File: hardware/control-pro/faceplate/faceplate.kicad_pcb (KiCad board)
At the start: 2 copper layers, 180 x 90 mm, 19 parts

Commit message: Enlarged 3rd slider slot width to remove copper from faceplate.
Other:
- board text added: "DMX-CPF, Rev 1.1 Crazy Giraffe Software"
- board text removed: "DMX-CPF, Rev 1.0 Crazy Giraffe Software"
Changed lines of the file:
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@@
     (title "DMX Demonstrator - Control-Pro Faceplate (DMX-CPF)")
     (date 2020-09-15)
-    (rev 1.0)
+    (rev 1.1)
     (company "Crazy Giraffe Software")
     (comment 2 "Designed by: SparkyBobo")
@@
     (fp_circle (center 0 0) (end 3.2 0) (layer Cmts.User) (width 0.15))
     (fp_circle (center 0 0) (end 3.45 0) (layer F.CrtYd) (width 0.05))
-    (pad "" np_thru_hole oval (at 0 6.25) (size 2.6 60) (drill oval 2 60) (layers *.Cu *.Mask))
+    (pad "" np_thru_hole oval (at 0 6.25) (size 2.6 60) (drill oval 2.6 60) (layers *.Cu *.Mask))
   )
   (module MountingHole:MountingHole_3.2mm_M3 (layer F.Cu)
@@
     (effects (font (size 1.5 1.5) (thickness 0.3)))
   )
-  (gr_text "DMX-CPF, Rev 1.0\nCrazy Giraffe Software" (at 240.75 72.25 90) (layer B.SilkS)
+  (gr_text "DMX-CPF, Rev 1.1\nCrazy Giraffe Software" (at 240.75 72.25 90) (layer B.SilkS)
     (effects (font (size 1 1) (thickness 0.15)) (justify mirror))
   )

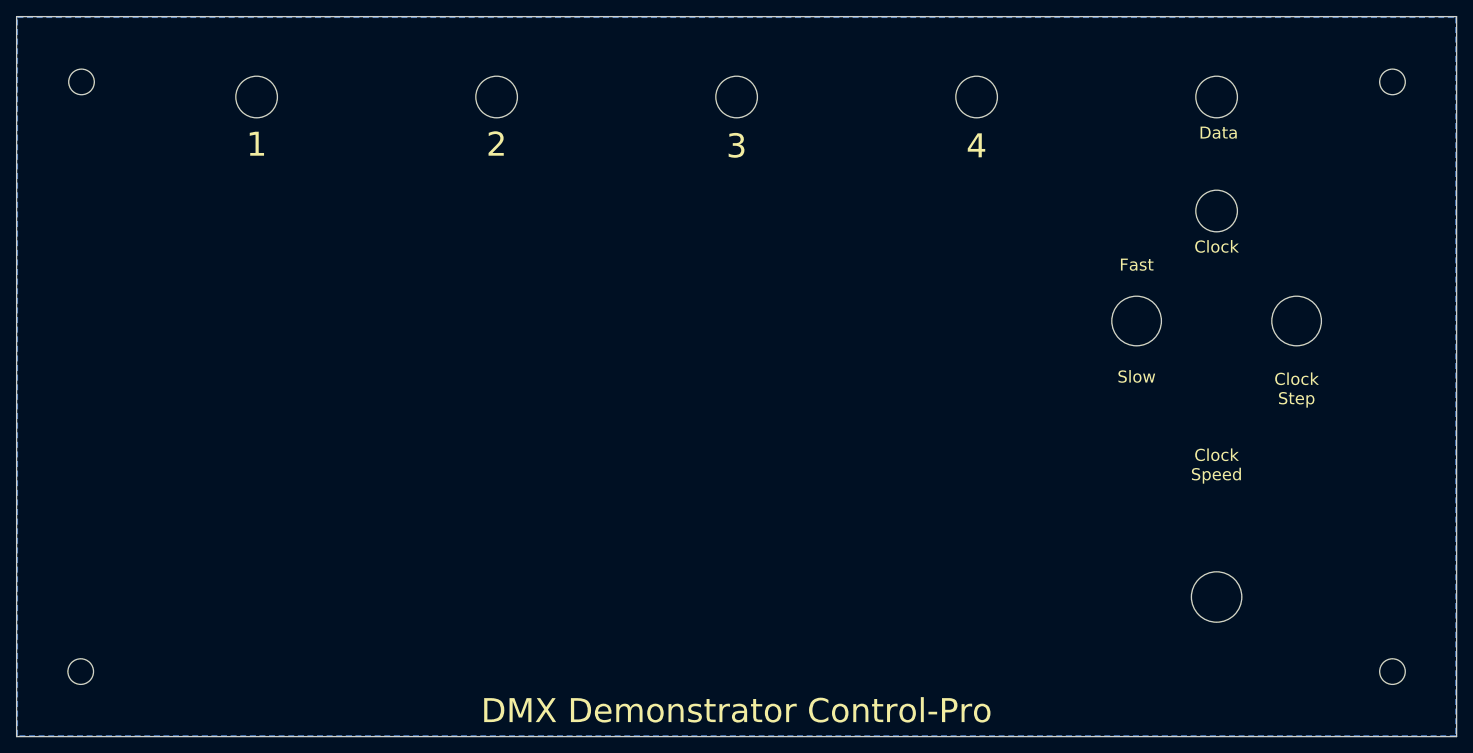
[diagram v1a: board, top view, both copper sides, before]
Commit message: Add rounded corners to control-pro.
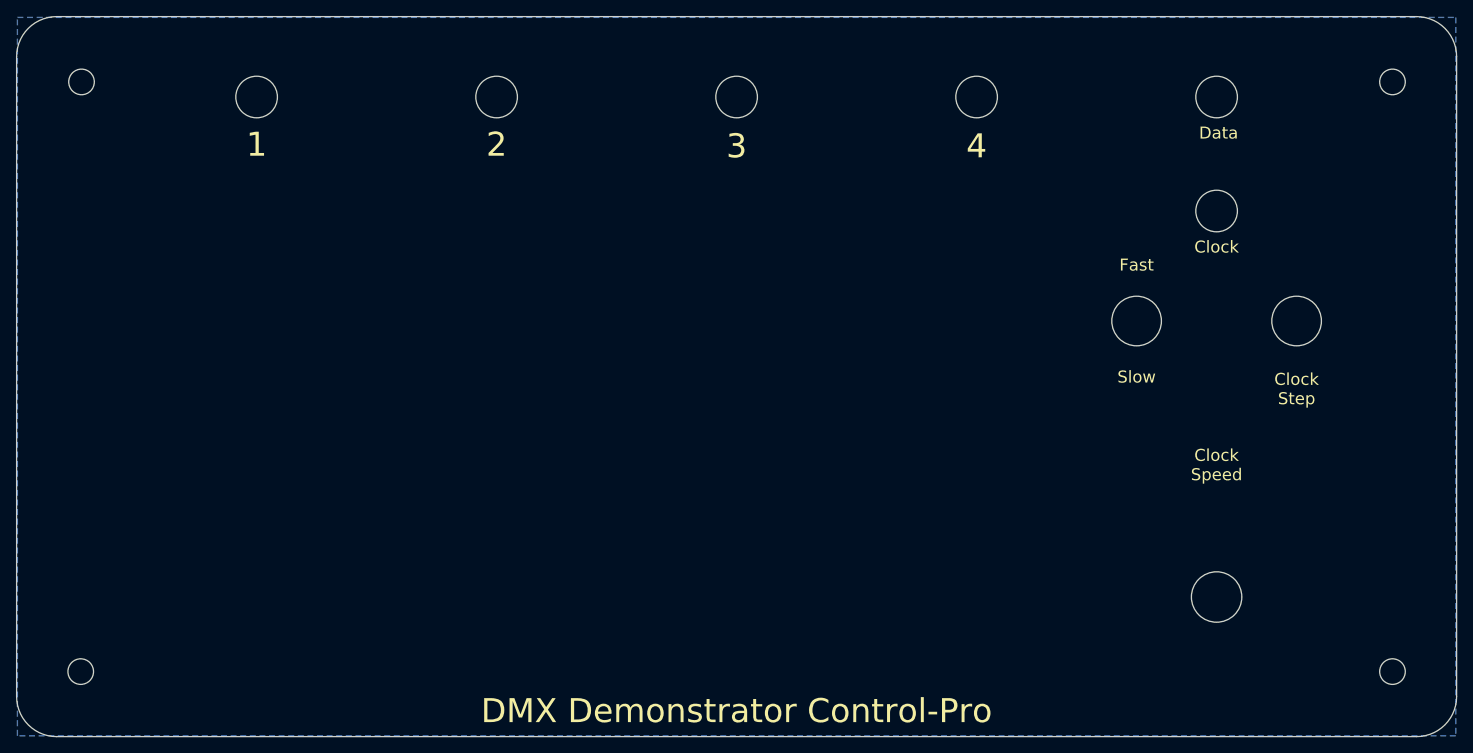
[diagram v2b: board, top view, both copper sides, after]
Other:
- outline, holes or cut-outs redrawn
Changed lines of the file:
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@@
   (general
     (thickness 1.6)
-    (drawings 103)
+    (drawings 111)
     (tracks 0)
     (zones 0)
@@
     (uvia_dia 0.3)
     (uvia_drill 0.1)
-    (add_net GND)
   )
   (module MountingHole:MountingHole_3.2mm_M3 (layer F.Cu)
@@
       (xy 0.4191 -0.20574) (xy 0.35814 -0.29972) (xy 0.27686 -0.37592) (xy 0.1778 -0.4318)) (layer B.SilkS) (width 0.01))
   )
+  (gr_line (start 69 139.2) (end 239 139.2) (layer Edge.Cuts) (width 0.1524))
+  (gr_line (start 64 54.2) (end 64 134.2) (layer Edge.Cuts) (width 0.1524))
+  (gr_line (start 239 49.2) (end 69 49.2) (layer Edge.Cuts) (width 0.1524))
+  (gr_line (start 244 134.2) (end 244 54.2) (layer Edge.Cuts) (width 0.1524))
+  (gr_arc (start 69 134.2) (end 64 134.2) (angle -90) (layer Edge.Cuts) (width 0.1524))
+  (gr_arc (start 69 54.2) (end 69 49.2) (angle -90) (layer Edge.Cuts) (width 0.1524))
+  (gr_arc (start 239 54.2) (end 244 54.2) (angle -90) (layer Edge.Cuts) (width 0.1524))
+  (gr_arc (start 239 134.2) (end 239 139.2) (angle -90) (layer Edge.Cuts) (width 0.1524))
+  (gr_line (start 239 49.2) (end 239 139.2) (layer Dwgs.User) (width 0.1524))
+  (gr_line (start 69 139.2) (end 69 49.2) (layer Dwgs.User) (width 0.1524))
+  (gr_line (start 64 134.2) (end 244 134.2) (layer Dwgs.User) (width 0.1524))
+  (gr_line (start 64 54.2) (end 244 54.2) (layer Dwgs.User) (width 0.1524))
   (gr_text "DMX Demonstrator Control-Pro" (at 154 136) (layer F.SilkS)
     (effects (font (size 3 3) (thickness 0.6)))
@@
   (gr_line (start 154 49.6) (end 154 139) (layer Dwgs.User) (width 0.1524))
   (gr_line (start 64.2 94.2) (end 243.8 94.2) (layer Dwgs.User) (width 0.1524))
-  (gr_line (start 64 139.2) (end 64 49.2) (layer Edge.Cuts) (width 0.1524))
-  (gr_line (start 244 139.2) (end 64 139.2) (layer Edge.Cuts) (width 0.1524))
-  (gr_line (start 244 49.2) (end 244 139.2) (layer Edge.Cuts) (width 0.1524))
-  (gr_line (start 64 49.2) (end 244 49.2) (layer Edge.Cuts) (width 0.1524))
   (gr_text "Clock\nStep" (at 224 95.75) (layer F.SilkS)
     (effects (font (size 1.5 1.5) (thickness 0.3)))
